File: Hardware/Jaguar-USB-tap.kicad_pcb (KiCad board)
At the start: 2 copper layers, 40 x 70 mm, 24 parts, among them J1 DB15, P1 CONN_01X03, P2 USB_B, P3 CONN_01X05, U1 NCP1117ST33T3G, U2 STM32F070F6, U3 TXB0106, U4 TXB0106, Y1 8MHz

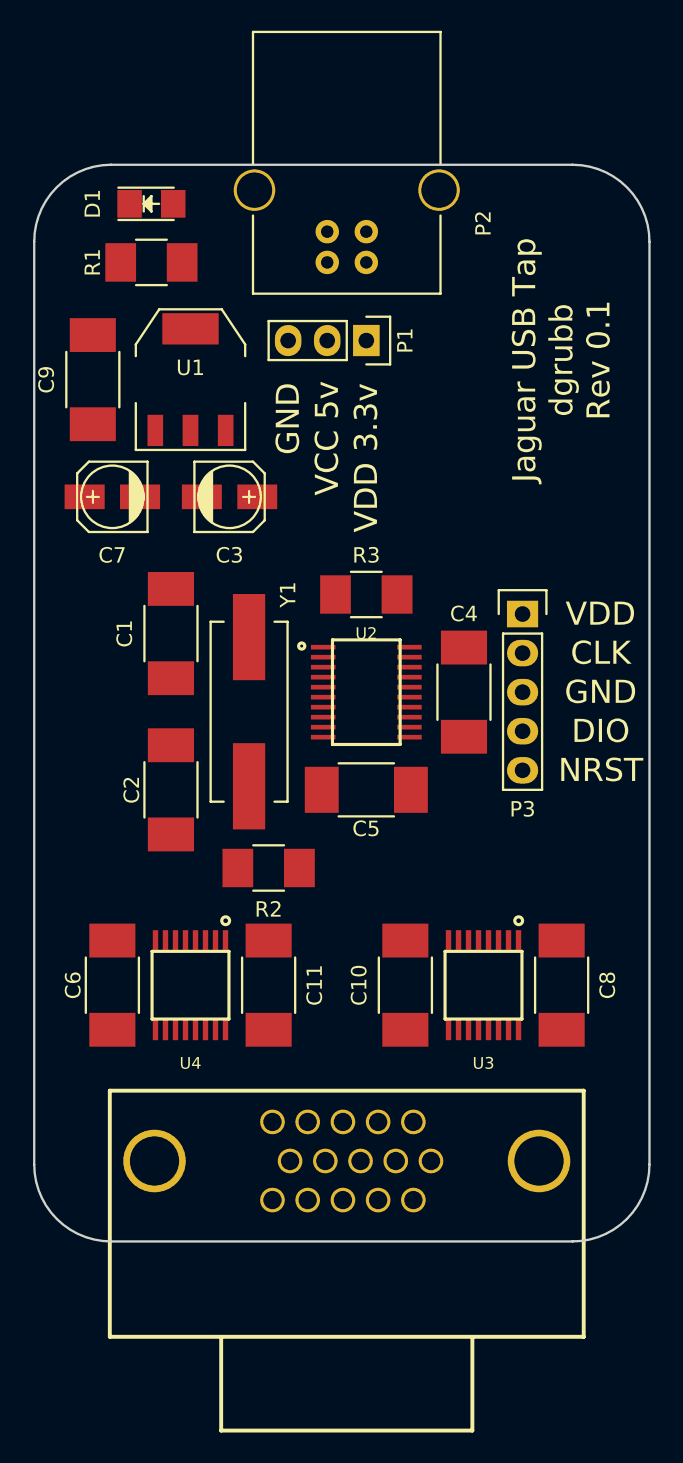
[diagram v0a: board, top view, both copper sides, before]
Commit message: Add traces and fill zones to PCB.
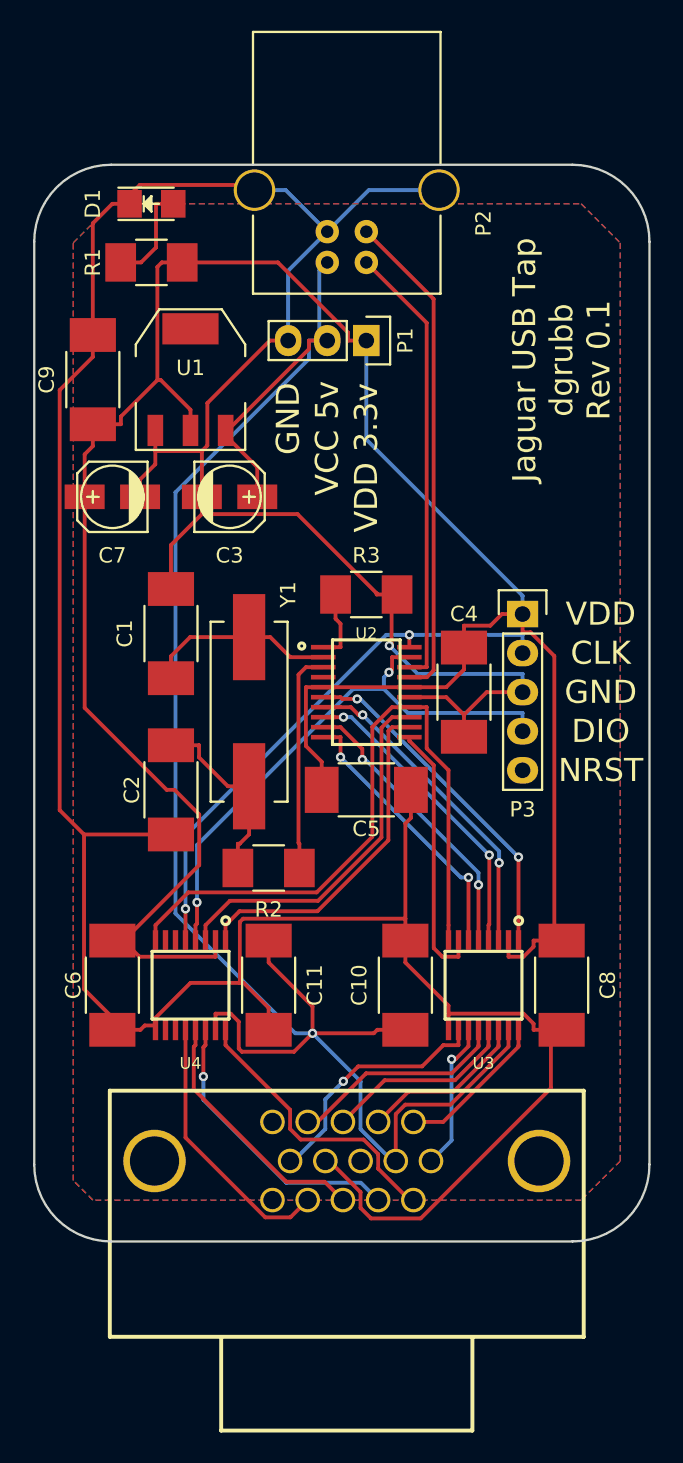
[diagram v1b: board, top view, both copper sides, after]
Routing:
- net GNDREF: track 0.00 -> 239.8 mm, vias 0 -> 1
- net VDD: track 0.00 -> 155.2 mm
- net VCC: track 0.00 -> 121.1 mm, vias 0 -> 1
- net OE: track 0.00 -> 44.5 mm
- net R5_VDD: track 0.00 -> 36.9 mm, vias 0 -> 2
- net R6_VDD: track 0.00 -> 36.2 mm, vias 0 -> 2
- net D-: track 0.00 -> 32.1 mm
- net D+: track 0.00 -> 29.1 mm
- net R4_VDD: track 0.00 -> 24.1 mm
- net R3_VDD: track 0.00 -> 22.5 mm
- net C1_VDD: track 0.00 -> 22.5 mm, vias 0 -> 2
- net C2_VDD: track 0.00 -> 21.2 mm, vias 0 -> 2
- net C3_VDD: track 0.00 -> 20.1 mm, vias 0 -> 2
- net C4_VDD: track 0.00 -> 18.9 mm, vias 0 -> 2
- net R4_VCC: track 0.00 -> 18.7 mm, vias 0 -> 1
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- added copper zone on B.Cu, net GNDREF
- added copper zone on F.Cu, net VDD
